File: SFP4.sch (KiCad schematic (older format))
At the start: 19 parts, among them J8 TYCO_1888247-1

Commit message: bugs fixed
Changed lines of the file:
@@
 $Descr A4 11693 8268
 encoding utf-8
-Sheet 12 25
+Sheet 11 25
 Title "Simple AFC"
 Date "2019-01-16"
@@
 Text Label 6550 1750 0    50   ~ 10
 SFP_4_TX_N
-Text HLabel 7400 1050 2    50   BiDi ~ 10
+Text HLabel 7400 1050 2    50   Output ~ 10
 SFP_4_RX_P
-Text HLabel 7400 1250 2    50   BiDi ~ 10
+Text HLabel 7400 1250 2    50   Output ~ 10
 SFP_4_RX_N
-Text HLabel 7400 1550 2    50   BiDi ~ 10
+Text HLabel 7400 1550 2    50   Input ~ 10
 SFP_4_TX_P
-Text HLabel 7400 1750 2    50   BiDi ~ 10
+Text HLabel 7400 1750 2    50   Input ~ 10
 SFP_4_TX_N
 Wire Wire Line

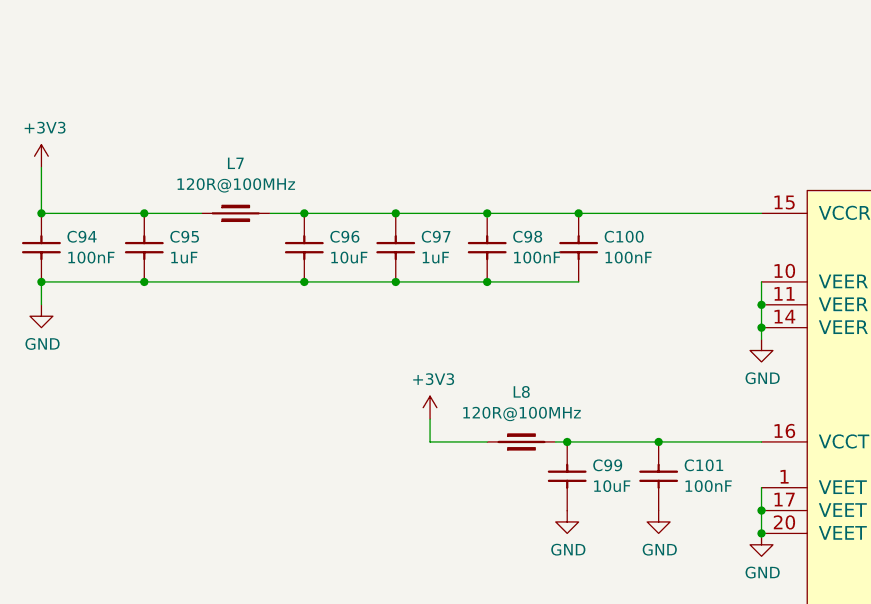
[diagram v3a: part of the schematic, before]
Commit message: SW2 placement changed, BOM cleared, FPGA boot, less ERC errors and wornings
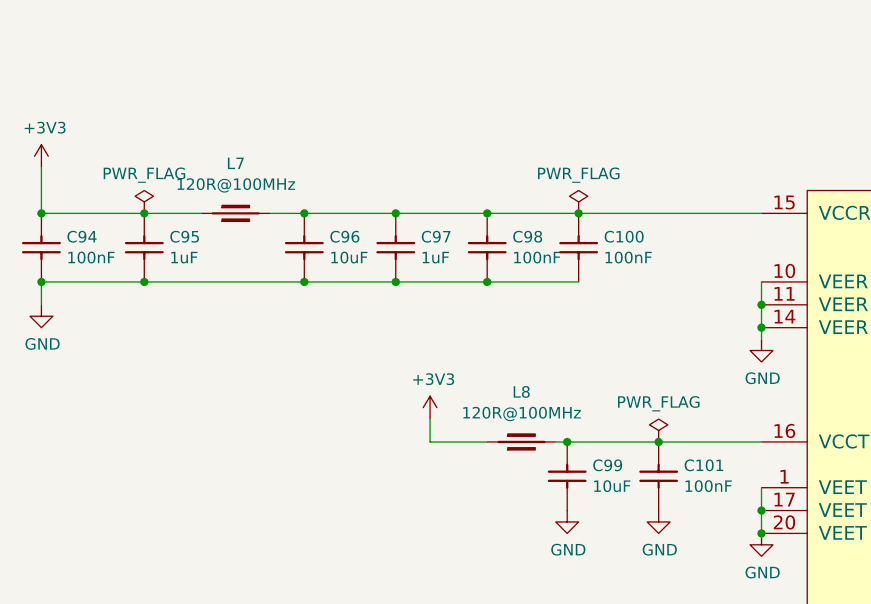
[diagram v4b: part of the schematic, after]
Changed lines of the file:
@@
 	4300 3250 4300 3350
 Connection ~ 4300 3350
+$Comp
+L power:PWR_FLAG #FLG?
+U 1 1 5D1E6ECD
+P 1600 1950
+AR Path="/5BABAC65/5D1E6ECD" Ref="#FLG?"  Part="1"
+AR Path="/5CC8AFE1/5D1E6ECD" Ref="#FLG0110"  Part="1"
+F 0 "#FLG0110" H 1600 2025 50  0001 C CNN
+F 1 "PWR_FLAG" H 1600 2123 50  0000 C CNN
+F 2 "" H 1600 1950 50  0001 C CNN
+F 3 "~" H 1600 1950 50  0001 C CNN
+	1    1600 1950
+	1    0    0    -1
+$EndComp
+$Comp
+L power:PWR_FLAG #FLG?
+U 1 1 5D1E8B75
+P 3500 1950
+AR Path="/5BABAC65/5D1E8B75" Ref="#FLG?"  Part="1"
+AR Path="/5CC8AFE1/5D1E8B75" Ref="#FLG0111"  Part="1"
+F 0 "#FLG0111" H 3500 2025 50  0001 C CNN
+F 1 "PWR_FLAG" H 3500 2123 50  0000 C CNN
+F 2 "" H 3500 1950 50  0001 C CNN
+F 3 "~" H 3500 1950 50  0001 C CNN
+	1    3500 1950
+	1    0    0    -1
+$EndComp
+$Comp
+L power:PWR_FLAG #FLG?
+U 1 1 5D1EA340
+P 3850 2950
+AR Path="/5BABAC65/5D1EA340" Ref="#FLG?"  Part="1"
+AR Path="/5CC8AFE1/5D1EA340" Ref="#FLG0112"  Part="1"
+F 0 "#FLG0112" H 3850 3025 50  0001 C CNN
+F 1 "PWR_FLAG" H 3850 3123 50  0000 C CNN
+F 2 "" H 3850 2950 50  0001 C CNN
+F 3 "~" H 3850 2950 50  0001 C CNN
+	1    3850 2950
+	1    0    0    -1
+$EndComp
 $EndSCHEMATC

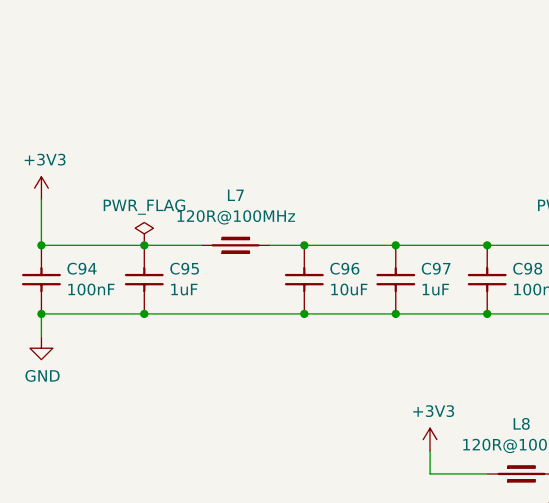
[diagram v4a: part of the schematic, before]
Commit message: README edited, less ERC errors and warnings
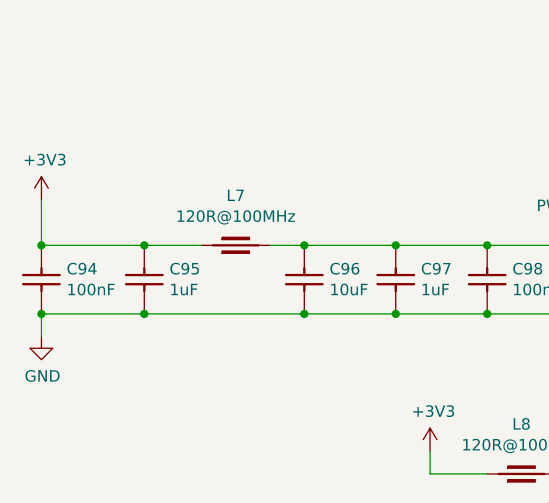
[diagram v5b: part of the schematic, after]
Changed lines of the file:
@@
 $Descr A4 11693 8268
 encoding utf-8
-Sheet 11 25
+Sheet 10 25
 Title "Marble"
 Date "2019-01-16"
@@
 $Comp
 L power:PWR_FLAG #FLG?
-U 1 1 5D1E6ECD
-P 1600 1950
-AR Path="/5BABAC65/5D1E6ECD" Ref="#FLG?"  Part="1"
-AR Path="/5CC8AFE1/5D1E6ECD" Ref="#FLG0110"  Part="1"
-F 0 "#FLG0110" H 1600 2025 50  0001 C CNN
-F 1 "PWR_FLAG" H 1600 2123 50  0000 C CNN
-F 2 "" H 1600 1950 50  0001 C CNN
-F 3 "~" H 1600 1950 50  0001 C CNN
-	1    1600 1950
-	1    0    0    -1
-$EndComp
-$Comp
-L power:PWR_FLAG #FLG?

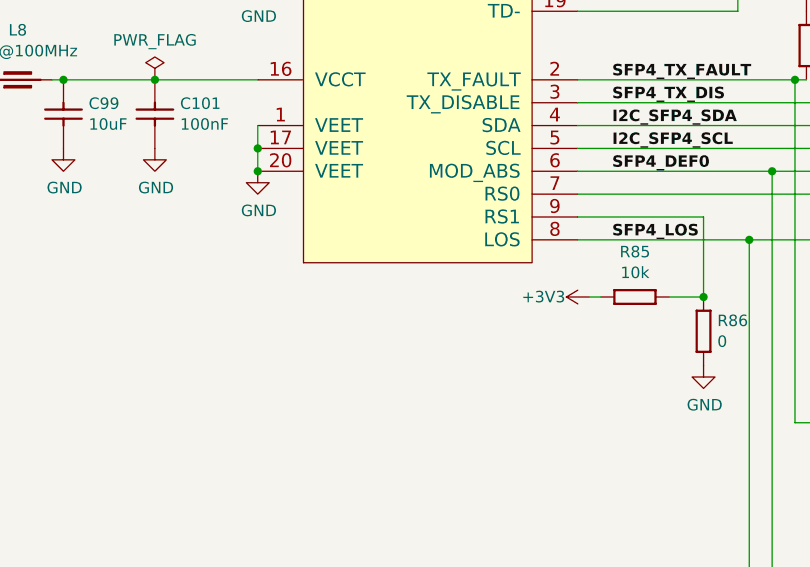
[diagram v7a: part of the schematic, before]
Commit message: SCH: shave down ERC to 1 error, 0 warning
  * 1 unavoidable error due to the unpopulated crystal Y2
  * change many pin types in symbol libraries (also for FMC con.)
  * as a result, could remove some power flags
  * fix footrint attribute for SFP module symbols

for most devices (not voltage regulators):
  * vcc = power input
  * gnd = power input
  * gpios (also FMC lanes) = bidirectional
  * configuration pins (tied to vcc / gnd) = inputs
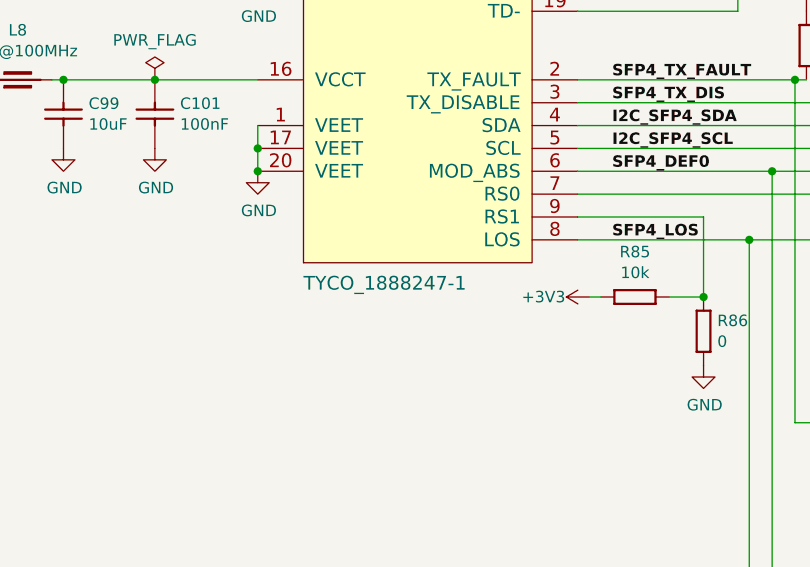
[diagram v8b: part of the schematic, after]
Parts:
- J8: footprint 1888247-1:TE_1888247-1 -> Marble:TE_1888247-1; Case ~~ -> (none); Comment ~~ -> (none); ComponentLink1Description ~~ -> (none); ComponentLink2Description ~~ -> (none); Database Table Name (none) -> TYCO; Device ~~ -> (none); Footprint Library (none) -> TYCO SMD; Library Name TYCO SMD -> Connectors.DbLib; PackageDescription ~~ -> (none); SCEM ~~ -> (none); Sense Comment ~~ -> (none); Status Comment ~~ -> (none)
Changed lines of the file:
@@
 AR Path="/5CC8AFE1/5C88E13D" Ref="J8"  Part="1"
 F 0 "J8" H 5000 2015 50  0000 C CNN
-F 1 "TYCO_1888247-1" H 4500 -140 60  0001 L CNN
-F 2 "1888247-1:TE_1888247-1" H 4500 -950 60  0001 L CNN
+F 1 "TYCO_1888247-1" H 4500 -140 60  0000 L CNN
+F 2 "Marble:TE_1888247-1" H 4500 -950 60  0001 L CNN
 F 3 "" H 4500 -320 60  0001 L CNN
 F 4 "SFP+" H 5000 1924 50  0000 C CNN "~"
@@
 F 6 "SFP+x1" H 4500 -500 60  0001 L CNN "Library Ref"
 F 7 "SchLib\\Connectors.SchLib" H 4500 -590 60  0001 L CNN "Library Path"
-F 8 "~~" H 4500 -680 60  0001 L CNN "Comment"
+F 8 " " H 4500 -680 60  0001 L CNN "Comment"
 F 9 "Standard" H 4500 -770 60  0001 L CNN "Component Kind"
 F 10 "Standard" H 4500 -860 60  0001 L CNN "Component Type"
-F 11 "~~" H 4500 -1040 60  0001 L CNN "PackageDescription"
+F 11 " " H 4500 -1040 60  0001 L CNN "PackageDescription"
 F 12 "20" H 4500 -1130 60  0001 L CNN "Pin Count"
-F 13 "~~" H 4500 -1220 60  0001 L CNN "Case"
+F 13 " " H 4500 -1220 60  0001 L CNN "Case"
 F 14 "PcbLib\\TYCO SMD.PcbLib" H 4500 -1310 60  0001 L CNN "Footprint Path"
 F 15 "TYCO_1888247-1" H 4500 -1400 60  0001 L CNN "Footprint Ref"
@@
 F 20 "No" H 4500 -1850 60  0001 L CNN "PressFit"
 F 21 "No" H 4500 -1940 60  0001 L CNN "Sense"
-F 22 "~~" H 4500 -2030 60  0001 L CNN "Sense Comment"
+F 22 " " H 4500 -2030 60  0001 L CNN "Sense Comment"
 F 23 "None" H 4500 -2120 60  0001 L CNN "Status"
-F 24 "~~" H 4500 -2210 60  0001 L CNN "Status Comment"
-F 25 "~~" H 4500 -2300 60  0001 L CNN "SCEM"
-F 26 "~~" H 4500 -2390 60  0001 L CNN "Device"
+F 24 " " H 4500 -2210 60  0001 L CNN "Status Comment"
+F 25 " " H 4500 -2300 60  0001 L CNN "SCEM"
+F 26 " " H 4500 -2390 60  0001 L CNN "Device"
 F 27 "20 Position, Pitch 0.8mm SFP+ Receptacle (Small Form-factor Pluggable)" H 4500 -2480 60  0001 L CNN "Part Description"
 F 28 "TYCO ELECTRONICS" H 4500 -2570 60  0001 L CNN "Manufacturer"
@@
 F 30 "5.4mm" H 4500 -2750 60  0001 L CNN "ComponentHeight"
 F 31 "~~" H 4500 -2840 60  0001 L CNN "ComponentLink1URL"
-F 32 "~~" H 4500 -2930 60  0001 L CNN "ComponentLink1Description"
+F 32 " " H 4500 -2930 60  0001 L CNN "ComponentLink1Description"
 F 33 "~~" H 4500 -3020 60  0001 L CNN "ComponentLink2URL"
-F 34 "~~" H 4500 -3110 60  0001 L CNN "ComponentLink2Description"
+F 34 " " H 4500 -3110 60  0001 L CNN "ComponentLink2Description"
 F 35 "\\\\cern.ch\\dfs\\Applications\\Altium\\Datasheets\\TYCO_1888247-1.pdf" H 4500 -3200 60  0001 L CNN "HelpURL"
 F 36 "CERN DEM JLC" H 4500 -3290 60  0001 L CNN "Author"
 F 37 "02/27/12 00:00:00" H 4500 -3380 60  0001 L CNN "CreateDate"
 F 38 "02/27/12 00:00:00" H 4500 -3470 60  0001 L CNN "LatestRevisionDate"
-F 39 "TYCO SMD" H 4500 -3560 60  0001 L CNN "Library Name"
+F 39 "Connectors.DbLib" H 4500 -3560 60  0001 L CNN "Library Name"
 F 40 "This work is licensed under the Creative Commons CC-BY-SA 4.0 License. To the extent that circuit schematics that use Licensed Material can be considered to be ‘Adapted Material’, then the copyright holder waives article 3.b of the license with respect to these schematics." H 4500 -3650 60  0001 L CNN "License"
+F 41 "TYCO" H 4500 1850 50  0001 C CNN "Database Table Name"
+F 42 "TYCO SMD" H 4500 1850 50  0001 C CNN "Footprint Library"
 	1    4500 1850
 	1    0    0    -1
